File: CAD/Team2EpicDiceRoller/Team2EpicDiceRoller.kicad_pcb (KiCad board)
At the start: 2 copper layers, 90 x 110 mm, 77 parts, among them J1 Conn_02x03_Odd_Even, J2 Conn_01x16, J3 Barrel_Jack, Q1 BSS138, SW1 SW_Toggle_SPDT, SW2 Tilt_Switch, SW3 SW_Power, SW4 RotaryEncoder_Switch, SW5 SW_LeftMenu, SW6 SW_MidMenu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

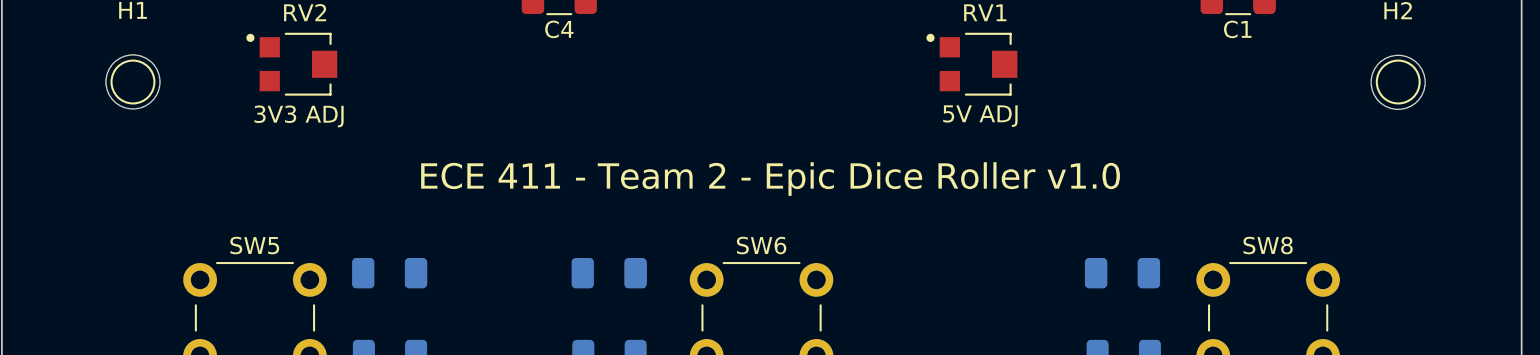
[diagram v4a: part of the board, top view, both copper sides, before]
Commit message: Added date to pcb
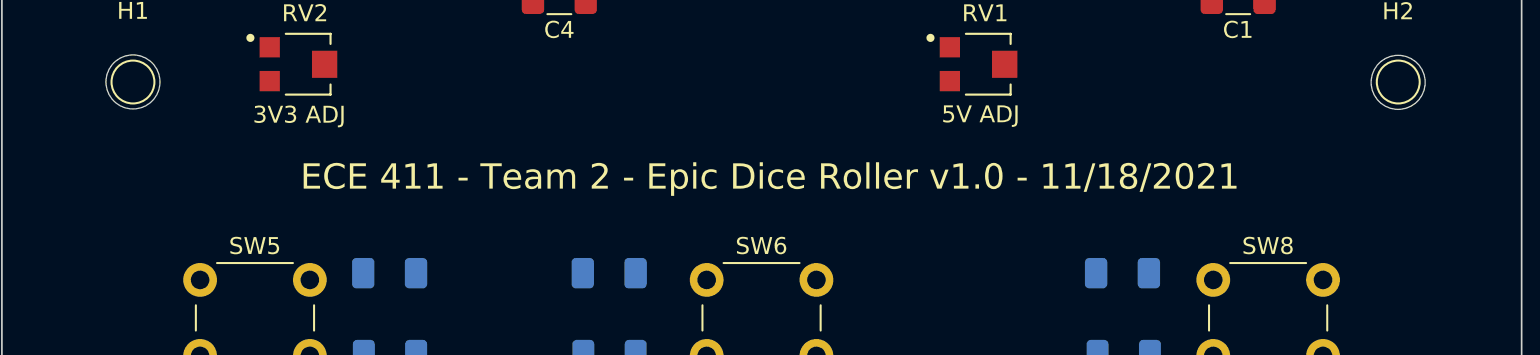
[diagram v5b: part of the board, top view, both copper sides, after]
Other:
- board text added: "ECE 411 - Team 2 - Epic Dice Roller v1.0 - 11/18/2021"
- board text removed: "ECE 411 - Team 2 - Epic Dice Roller v1.0"
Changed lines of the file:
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@@
     (effects (font (size 1 1) (thickness 0.15)))
   )
-  (gr_text "ECE 411 - Team 2 - Epic Dice Roller v1.0" (at 142.5 61.5) (layer "F.SilkS")
+  (gr_text "ECE 411 - Team 2 - Epic Dice Roller v1.0 - 11/18/2021" (at 142.5 61.5) (layer "F.SilkS")
     (effects (font (size 1.5 1.5) (thickness 0.3)))
   )

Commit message: Updated pcb with those changes
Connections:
- U2 pad 1: /LeftDebn -> /RigDebn
- U2 pad 2: IO5_PD5 -> AD0_PC0
- U2 pad 3: /MidDebn -> /LeftDebn
- U2 pad 4: IO6_PD6 -> IO5_PD5
- U2 pad 5: /RigDebn -> /MidDebn
- U2 pad 6: IO10_SS_PB2 -> IO6_PD6

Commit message: minor changes to text
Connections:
- U2 pad 2: AD0_PC0 -> AD1_PC1
- U2 pad 8: IO4_PD4 -> AD0_PC0
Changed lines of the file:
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@@
       (net 63 "/RigDebn") (pintype "input"))
     (pad "2" smd roundrect locked (at -2.475 2.54 270) (size 1.95 0.6) (layers "B.Cu" "B.Paste" "B.Mask") (roundrect_rratio 0.25)
-      (net 29 "AD0_PC0") (pintype "output"))
+      (net 28 "AD1_PC1") (pintype "output"))
     (pad "3" smd roundrect locked (at -2.475 1.27 270) (size 1.95 0.6) (layers "B.Cu" "B.Paste" "B.Mask") (roundrect_rratio 0.25)
       (net 61 "/LeftDebn") (pintype "input"))
@@
       (net 1 "GND") (pinfunction "GND") (pintype "power_in"))
     (pad "8" smd roundrect locked (at 2.475 -3.81 270) (size 1.95 0.6) (layers "B.Cu" "B.Paste" "B.Mask") (roundrect_rratio 0.25)
-      (net 35 "IO4_PD4") (pintype "output"))
+      (net 29 "AD0_PC0") (pintype "output"))
     (pad "9" smd roundrect locked (at 2.475 -2.54 270) (size 1.95 0.6) (layers "B.Cu" "B.Paste" "B.Mask") (roundrect_rratio 0.25)
       (net 60 "/EncDebnc") (pintype "input"))

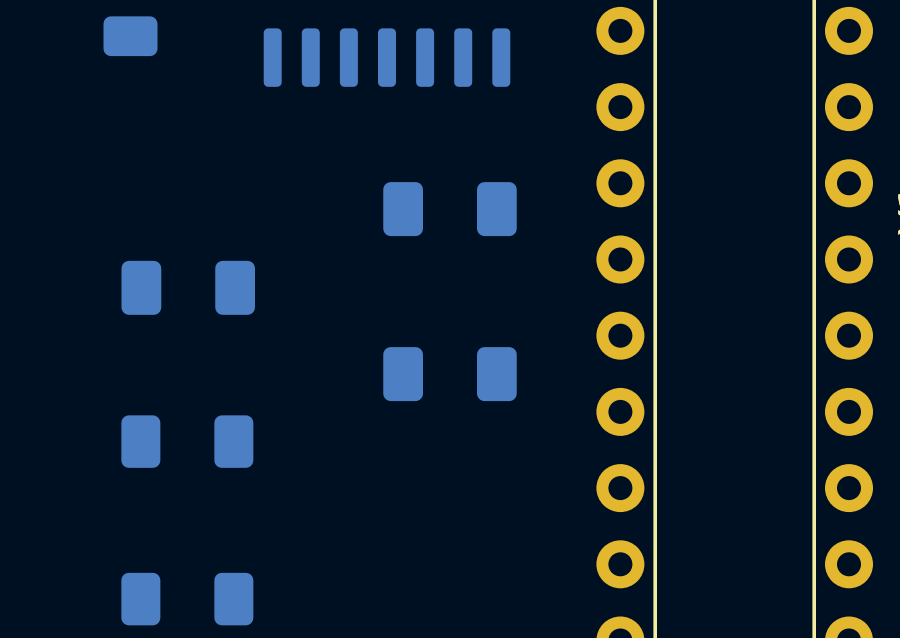
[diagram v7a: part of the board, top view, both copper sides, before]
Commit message: flipped a few capacitors
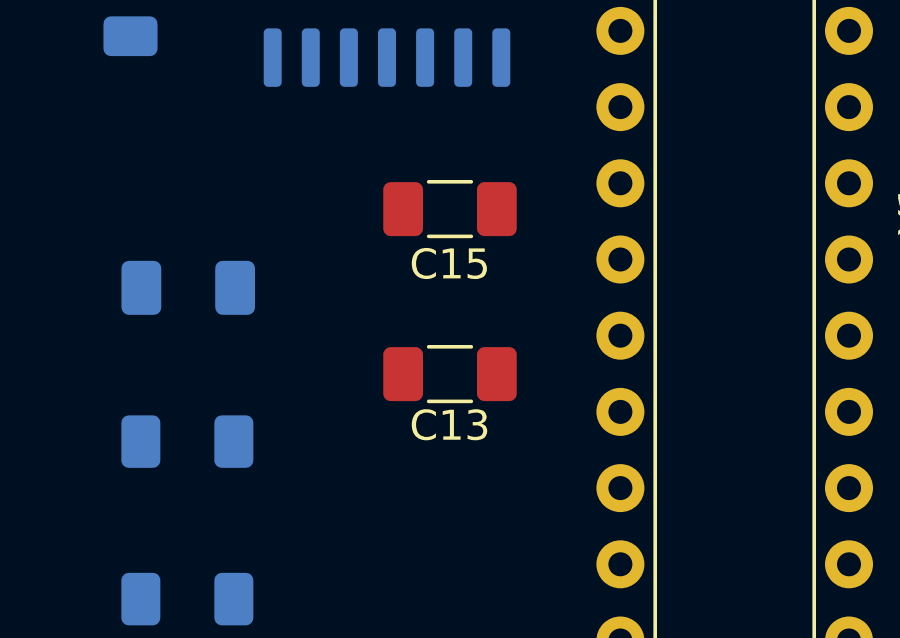
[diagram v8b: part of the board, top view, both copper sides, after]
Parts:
- C13, C15: moved to F.Cu
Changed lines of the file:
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@@
+    )
+  )
+  (footprint "Capacitor_SMD:C_1206_3216Metric_Pad1.33x1.80mm_HandSolder" (layer "F.Cu")
+    (at 132.5 99)
+    (descr "Capacitor SMD 1206 (3216 Metric), square (rectangular) end terminal, IPC_7351 nominal with elongated pad for handsoldering. (Body size source: IPC-SM-782 page 76, https://www.pcb-3d.com/wordpress/wp-content/uploads/ipc-sm-782a_amendment_1_and_2.pdf), generated with kicad-footprint-generator")
+    (tags "capacitor handsolder")
+    (property "Sheetfile" "Team2EpicDiceRoller.kicad_sch")
+    (property "Sheetname" "")
+    (attr smd)
+    (fp_text reference "C15" (at 0 1.85) (layer "F.SilkS")
+      (effects (font (size 1 1) (thickness 0.15)))
+    )
+    (fp_text value "100n" (at 0 -1.925) (layer "F.Fab")
+      (effects (font (size 1 1) (thickness 0.15)))
+    )
+    (fp_text user "${REFERENCE}" (at 0 0) (layer "F.Fab")
+      (effects (font (size 0.8 0.8) (thickness 0.12)))
+    )
+    (fp_line (start -0.711252 0.91) (end 0.711252 0.91) (layer "F.SilkS") (width 0.12))
+    (fp_line (start -0.711252 -0.91) (end 0.711252 -0.91) (layer "F.SilkS") (width 0.12))
+    (fp_line (start 2.48 1.15) (end -2.48 1.15) (layer "F.CrtYd") (width 0.05))
+    (fp_line (start 2.48 -1.15) (end 2.48 1.15) (layer "F.CrtYd") (width 0.05))
+    (fp_line (start -2.48 -1.15) (end 2.48 -1.15) (layer "F.CrtYd") (width 0.05))
+    (fp_line (start -2.48 1.15) (end -2.48 -1.15) (layer "F.CrtYd") (width 0.05))
+    (fp_line (start -1.6 0.8) (end -1.6 -0.8) (layer "F.Fab") (width 0.1))
+    (fp_line (start 1.6 -0.8) (end 1.6 0.8) (layer "F.Fab") (width 0.1))
+    (fp_line (start -1.6 -0.8) (end 1.6 -0.8) (layer "F.Fab") (width 0.1))
+    (fp_line (start 1.6 0.8) (end -1.6 0.8) (layer "F.Fab") (width 0.1))
+    (pad "1" smd roundrect locked (at -1.5625 0) (size 1.325 1.8) (layers "F.Cu" "F.Paste" "F.Mask") (roundrect_rratio 0.188679)
+      (net 1 "GND") (pintype "passive"))
+    (pad "2" smd roundrect locked (at 1.5625 0) (size 1.325 1.8) (layers "F.Cu" "F.Paste" "F.Mask") (roundrect_rratio 0.188679)
+      (net 4 "VCC") (pintype "passive"))
+    (model "${KICAD6_3DMODEL_DIR}/Capacitor_SMD.3dshapes/C_1206_3216Metric.wrl"
+      (offset (xyz 0 0 0))
+      (scale (xyz 1 1 1))
+      (rotate (xyz 0 0 0))
     )
   )
@@
     (fp_circle (center 0 0) (end 3.45 0) (layer "F.CrtYd") (width 0.05) (fill none))
     (pad "" np_thru_hole circle locked (at 0 0) (size 3.2 3.2) (drill 3.2) (layers *.Cu *.Mask))
+  )
+  (footprint "Capacitor_SMD:C_1206_3216Metric_Pad1.33x1.80mm_HandSolder" (layer "F.Cu")
+    (at 132.5 104.5)
+    (descr "Capacitor SMD 1206 (3216 Metric), square (rectangular) end terminal, IPC_7351 nominal with elongated pad for handsoldering. (Body size source: IPC-SM-782 page 76, https://www.pcb-3d.com/wordpress/wp-content/uploads/ipc-sm-782a_amendment_1_and_2.pdf), generated with kicad-footprint-generator")
+    (tags "capacitor handsolder")
+    (property "Sheetfile" "Team2EpicDiceRoller.kicad_sch")
+    (property "Sheetname" "")
+    (attr smd)
+    (fp_text reference "C13" (at 0 1.725) (layer "F.SilkS")
+      (effects (font (size 1 1) (thickness 0.15)))
+    )
+    (fp_text value "100n" (at -0.075 -1.9) (layer "F.Fab")
+      (effects (font (size 1 1) (thickness 0.15)))
+    )
+    (fp_text user "${REFERENCE}" (at 0 0) (layer "F.Fab")
+      (effects (font (size 0.8 0.8) (thickness 0.12)))
+    )
+    (fp_line (start -0.711252 0.91) (end 0.711252 0.91) (layer "F.SilkS") (width 0.12))
+    (fp_line (start -0.711252 -0.91) (end 0.711252 -0.91) (layer "F.SilkS") (width 0.12))
+    (fp_line (start 2.48 -1.15) (end 2.48 1.15) (layer "F.CrtYd") (width 0.05))
+    (fp_line (start -2.48 1.15) (end -2.48 -1.15) (layer "F.CrtYd") (width 0.05))
+    (fp_line (start -2.48 -1.15) (end 2.48 -1.15) (layer "F.CrtYd") (width 0.05))
+    (fp_line (start 2.48 1.15) (end -2.48 1.15) (layer "F.CrtYd") (width 0.05))
+    (fp_line (start -1.6 -0.8) (end 1.6 -0.8) (layer "F.Fab") (width 0.1))
+    (fp_line (start 1.6 0.8) (end -1.6 0.8) (layer "F.Fab") (width 0.1))
+    (fp_line (start -1.6 0.8) (end -1.6 -0.8) (layer "F.Fab") (width 0.1))
+    (fp_line (start 1.6 -0.8) (end 1.6 0.8) (layer "F.Fab") (width 0.1))
+    (pad "1" smd roundrect locked (at -1.5625 0) (size 1.325 1.8) (layers "F.Cu" "F.Paste" "F.Mask") (roundrect_rratio 0.188679)
+      (net 1 "GND") (pintype "passive"))
+    (pad "2" smd roundrect locked (at 1.5625 0) (size 1.325 1.8) (layers "F.Cu" "F.Paste" "F.Mask") (roundrect_rratio 0.188679)
+      (net 49 "Net-(C13-Pad2)") (pintype "passive"))
+    (model "${KICAD6_3DMODEL_DIR}/Capacitor_SMD.3dshapes/C_1206_3216Metric.wrl"
+      (offset (xyz 0 0 0))
+      (scale (xyz 1 1 1))
+      (rotate (xyz 0 0 0))
+    )
   )
   (footprint "Library:TRIM_TC33X-2-502E" (layer "F.Cu")
@@
   )
   (footprint "Capacitor_SMD:C_1206_3216Metric_Pad1.33x1.80mm_HandSolder" (layer "B.Cu")
-    (at 132.5 99)
-    (descr "Capacitor SMD 1206 (3216 Metric), square (rectangular) end terminal, IPC_7351 nominal with elongated pad for handsoldering. (Body size source: IPC-SM-782 page 76, https://www.pcb-3d.com/wordpress/wp-content/uploads/ipc-sm-782a_amendment_1_and_2.pdf), generated with kicad-footprint-generator")
-    (tags "capacitor handsolder")
-    (property "Sheetfile" "Team2EpicDiceRoller.kicad_sch")
-    (property "Sheetname" "")
-    (attr smd)
-    (fp_text reference "C15" (at 0 -1.85) (layer "B.SilkS")
-      (effects (font (size 1 1) (thickness 0.15)) (justify mirror))
-    )
-    (fp_text value "100n" (at 0 1.925) (layer "B.Fab")
-      (effects (font (size 1 1) (thickness 0.15)) (justify mirror))
-    )
-    (fp_text user "${REFERENCE}" (at 0 0) (layer "B.Fab")
-      (effects (font (size 0.8 0.8) (thickness 0.12)) (justify mirror))
-    )
-    (fp_line (start -0.711252 -0.91) (end 0.711252 -0.91) (layer "B.SilkS") (width 0.12))
-    (fp_line (start -0.711252 0.91) (end 0.711252 0.91) (layer "B.SilkS") (width 0.12))
-    (fp_line (start 2.48 -1.15) (end -2.48 -1.15) (layer "B.CrtYd") (width 0.05))
-    (fp_line (start 2.48 1.15) (end 2.48 -1.15) (layer "B.CrtYd") (width 0.05))
-    (fp_line (start -2.48 1.15) (end 2.48 1.15) (layer "B.CrtYd") (width 0.05))
-    (fp_line (start -2.48 -1.15) (end -2.48 1.15) (layer "B.CrtYd") (width 0.05))
-    (fp_line (start -1.6 -0.8) (end -1.6 0.8) (layer "B.Fab") (width 0.1))
-    (fp_line (start 1.6 0.8) (end 1.6 -0.8) (layer "B.Fab") (width 0.1))
-    (fp_line (start -1.6 0.8) (end 1.6 0.8) (layer "B.Fab") (width 0.1))
-    (fp_line (start 1.6 -0.8) (end -1.6 -0.8) (layer "B.Fab") (width 0.1))
-    (pad "1" smd roundrect locked (at -1.5625 0) (size 1.325 1.8) (layers "B.Cu" "B.Paste" "B.Mask") (roundrect_rratio 0.188679)
-      (net 1 "GND") (pintype "passive"))
-    (pad "2" smd roundrect locked (at 1.5625 0) (size 1.325 1.8) (layers "B.Cu" "B.Paste" "B.Mask") (roundrect_rratio 0.188679)
-      (net 4 "VCC") (pintype "passive"))
-    (model "${KICAD6_3DMODEL_DIR}/Capacitor_SMD.3dshapes/C_1206_3216Metric.wrl"
-      (offset (xyz 0 0 0))
-      (scale (xyz 1 1 1))
-      (rotate (xyz 0 0 0))
-    )
-  )
-  (footprint "Capacitor_SMD:C_1206_3216Metric_Pad1.33x1.80mm_HandSolder" (layer "B.Cu")
     (at 151.575 111.675 180)
     (descr "Capacitor SMD 1206 (3216 Metric), square (rectangular) end terminal, IPC_7351 nominal with elongated pad for handsoldering. (Body size source: IPC-SM-782 page 76, https://www.pcb-3d.com/wordpress/wp-content/uploads/ipc-sm-782a_amendment_1_and_2.pdf), generated with kicad-footprint-generator")
@@
     (model "${KICAD6_3DMODEL_DIR}/Capacitor_SMD.3dshapes/C_1206_3216Metric.wrl"
       (offset (xyz 0 0 0))
-      (scale (xyz 1 1 1))
-      (rotate (xyz 0 0 0))
-    )
-  )
-  (footprint "Capacitor_SMD:C_1206_3216Metric_Pad1.33x1.80mm_HandSolder" (layer "B.Cu")
-    (at 132.5 104.5)
-    (descr "Capacitor SMD 1206 (3216 Metric), square (rectangular) end terminal, IPC_7351 nominal with elongated pad for handsoldering. (Body size source: IPC-SM-782 page 76, https://www.pcb-3d.com/wordpress/wp-content/uploads/ipc-sm-782a_amendment_1_and_2.pdf), generated with kicad-footprint-generator")
-    (tags "capacitor handsolder")
-    (property "Sheetfile" "Team2EpicDiceRoller.kicad_sch")
-    (property "Sheetname" "")
-    (attr smd)
-    (fp_text reference "C13" (at 0 -1.725) (layer "B.SilkS")
-      (effects (font (size 1 1) (thickness 0.15)) (justify mirror))
-    )
-    (fp_text value "100n" (at -0.075 1.9) (layer "B.Fab")
-      (effects (font (size 1 1) (thickness 0.15)) (justify mirror))
-    )
-    (fp_text user "${REFERENCE}" (at 0 0) (layer "B.Fab")
-      (effects (font (size 0.8 0.8) (thickness 0.12)) (justify mirror))
-    )
-    (fp_line (start -0.711252 -0.91) (end 0.711252 -0.91) (layer "B.SilkS") (width 0.12))
-    (fp_line (start -0.711252 0.91) (end 0.711252 0.91) (layer "B.SilkS") (width 0.12))
-    (fp_line (start 2.48 1.15) (end 2.48 -1.15) (layer "B.CrtYd") (width 0.05))
-    (fp_line (start -2.48 -1.15) (end -2.48 1.15) (layer "B.CrtYd") (width 0.05))
-    (fp_line (start -2.48 1.15) (end 2.48 1.15) (layer "B.CrtYd") (width 0.05))
-    (fp_line (start 2.48 -1.15) (end -2.48 -1.15) (layer "B.CrtYd") (width 0.05))
-    (fp_line (start -1.6 0.8) (end 1.6 0.8) (layer "B.Fab") (width 0.1))
-    (fp_line (start 1.6 -0.8) (end -1.6 -0.8) (layer "B.Fab") (width 0.1))
-    (fp_line (start -1.6 -0.8) (end -1.6 0.8) (layer "B.Fab") (width 0.1))
-    (fp_line (start 1.6 0.8) (end 1.6 -0.8) (layer "B.Fab") (width 0.1))
-    (pad "1" smd roundrect locked (at -1.5625 0) (size 1.325 1.8) (layers "B.Cu" "B.Paste" "B.Mask") (roundrect_rratio 0.188679)
-      (net 1 "GND") (pintype "passive"))
-    (pad "2" smd roundrect locked (at 1.5625 0) (size 1.325 1.8) (layers "B.Cu" "B.Paste" "B.Mask") (roundrect_rratio 0.188679)
-      (net 49 "Net-(C13-Pad2)") (pintype "passive"))
-    (model "${KICAD6_3DMODEL_DIR}/Capacitor_SMD.3dshapes/C_1206_3216Metric.wrl"
-      (offset (xyz 0 0 0))
